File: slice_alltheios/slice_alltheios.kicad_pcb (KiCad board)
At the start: 2 copper layers, 9.5 x 26.7 mm, 2 parts, among them J1 Conn_01x21, J2 Conn_02x10_Odd_Even

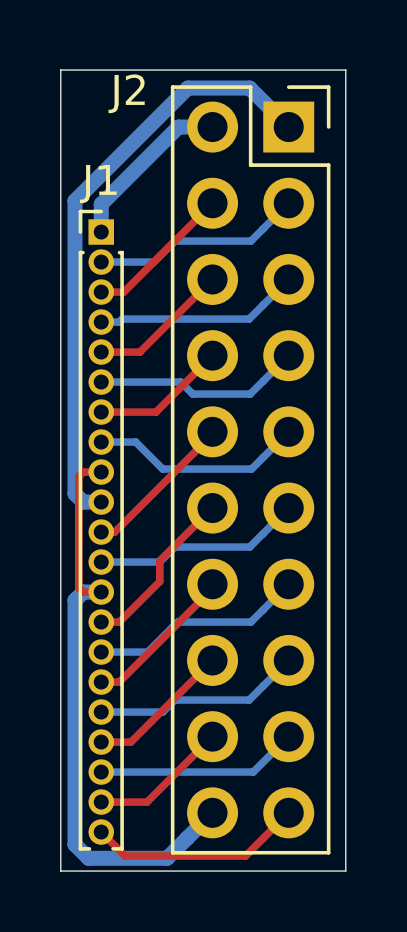
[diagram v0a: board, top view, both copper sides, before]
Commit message: Fix solder mask.
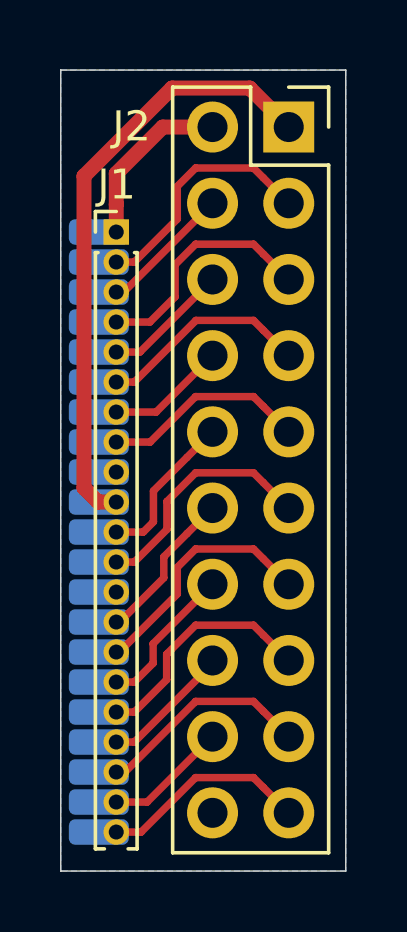
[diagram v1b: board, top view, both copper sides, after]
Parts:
- J1: footprint Connector_PinHeader_1.00mm:PinHeader_1x21_P1.00mm_Vertical -> edgeconnector:breadbee_1mm_header_connector
- moved J1 0.50 mm to (145.8, 84.5)
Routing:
- net GND: track 19.9 -> 0.00 mm
- net /sd_d3: track 7.06 -> 8.17 mm
- net /sd_d1: track 6.84 -> 7.94 mm
- net /usb_dp: track 7.00 -> 8.01 mm
- net /sr_io14: track 7.19 -> 8.18 mm
- net /sr_io12: track 6.96 -> 7.93 mm
- net /sr_io9: track 4.61 -> 4.11 mm
- net /sd_d2: track 4.94 -> 4.44 mm
- net /sd_d0: track 4.71 -> 4.21 mm
- net /sd_clk: track 4.49 -> 3.99 mm
- added copper zone on B.Cu, net GND
